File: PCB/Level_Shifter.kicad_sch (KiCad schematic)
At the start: 5 parts, among them Q1 BSS138, Q2 BSS84

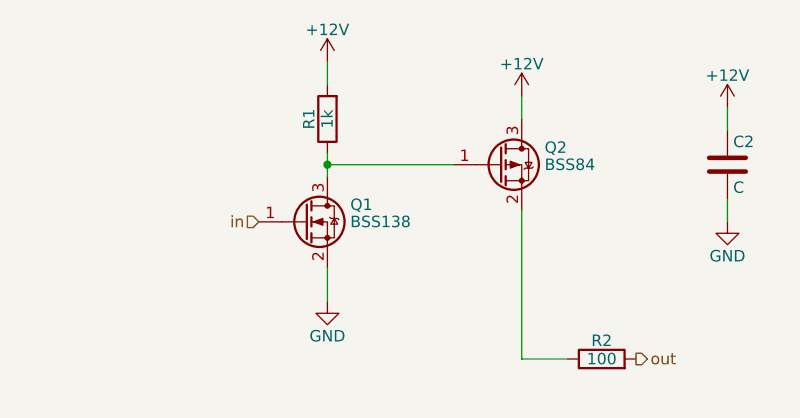
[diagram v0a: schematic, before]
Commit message: Fixed switched source and drain on PMOS
On 12V common source amp for level shifter in subcircuit
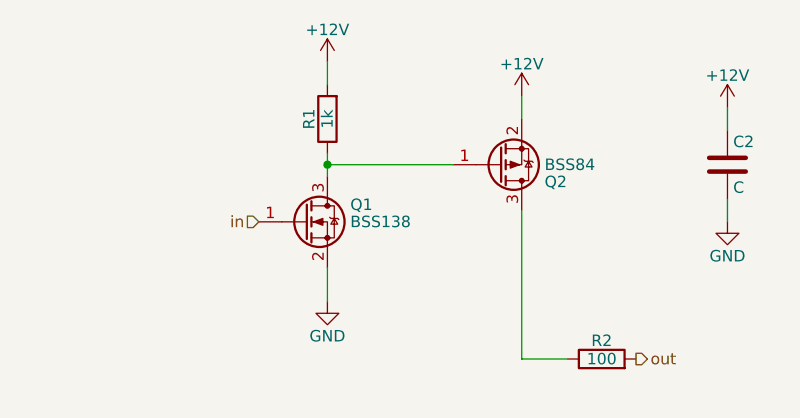
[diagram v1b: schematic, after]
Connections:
- net +12V: now also Q2.2 (S); no longer Q2.3 (D)
- net at R2.1: now also Q2.3 (D); no longer Q2.2 (S)

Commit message: Version 2 of PCB
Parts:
- added R15: 10k, Resistor_SMD:R_0805_2012Metric_Pad1.20x1.40mm_HandSolder, symbol Device:R
- C2: value C -> 10uF; JL Part# (none) -> C15850
- Q1: value BSS138 -> 2N7002; JL Part# (none) -> C8545
- Q2: value BSS84 -> AO3401A; JL Part# (none) -> C15127
- R1: JL Part# (none) -> C17513
- R2: JL Part# (none) -> C17408
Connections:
- net GND: now also R15.1
- net in: now also R15.2
